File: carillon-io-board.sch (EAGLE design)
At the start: 51 parts, among them J1 22-27-2031-03, J10 22-27-2031-03, J2 22-27-2031-03, J3 22-27-2031-03, J4 22-27-2031-03, J5 22-27-2031-03, J6 22-27-2031-03, J7 22-27-2031-03, J8 22-27-2031-03, J9 22-27-2031-03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

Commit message: fix board
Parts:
- removed R10, R12, R14, R16, R18, R2, R20, R4, R6, R8: (no value), resistor:R-EU_0207/10
- J1, J10, J2, J3, J4, J5, J6, J7, J8, J9: value 22-27-2031-03 -> 22-05-7048-04; device con-molex:22-27-2031-03 -> con-molex:22-05-7048-04
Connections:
- net 12V: now also J1-2.S, J10-2.S, J2-2.S, J3-2.S, J4-2.S, J5-2.S, J6-2.S, J7-2.S, J8-2.S, J9-2.S; no longer J1-1.S, J10-1.S, J2-1.S, J3-1.S, J4-1.S, J5-1.S, J6-1.S, J7-1.S, J8-1.S, J9-1.S
- net GND: now also J1-1.S, J10-1.S, J2-1.S, J3-1.S, J4-1.S, J5-1.S, J6-1.S, J7-1.S, J8-1.S, J9-1.S; no longer R10.2, R12.2, R14.2, R16.2, R18.2, R2.2, R20.2, R4.2, R6.2, R8.2
- net IN1: now also J1-3.S; no longer J1-2.S, R2.1
- net IN10: now also J10-3.S; no longer J10-2.S, R20.1
- net IN2: now also J2-3.S; no longer J2-2.S, R4.1
- net IN3: now also J3-3.S; no longer J3-2.S, R6.1
- net IN4: now also J4-3.S; no longer J4-2.S, R8.1
- net IN5: now also J5-3.S; no longer J5-2.S, R10.1
- net IN6: now also J6-3.S; no longer J6-2.S, R12.1
- net IN7: now also J7-3.S; no longer J7-2.S, R14.1
- net IN8: now also J8-3.S; no longer J8-2.S, R16.1
- net IN9: now also J9-3.S; no longer J9-2.S, R18.1
- net N$1: now also J1-4.S; no longer J1-3.S
- net N$10: now also J10-4.S; no longer J10-3.S
- net N$2: now also J6-4.S; no longer J6-3.S
- net N$3: now also J2-4.S; no longer J2-3.S
- net N$4: now also J3-4.S; no longer J3-3.S
- net N$5: now also J4-4.S; no longer J4-3.S
- net N$6: now also J5-4.S; no longer J5-3.S
- net N$7: now also J7-4.S; no longer J7-3.S
- net N$8: now also J8-4.S; no longer J8-3.S
- net N$9: now also J9-4.S; no longer J9-3.S

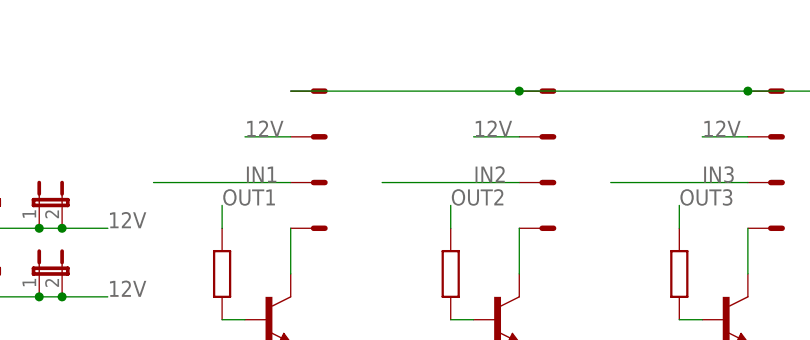
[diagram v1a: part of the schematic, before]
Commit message: io board proved, firmware file added
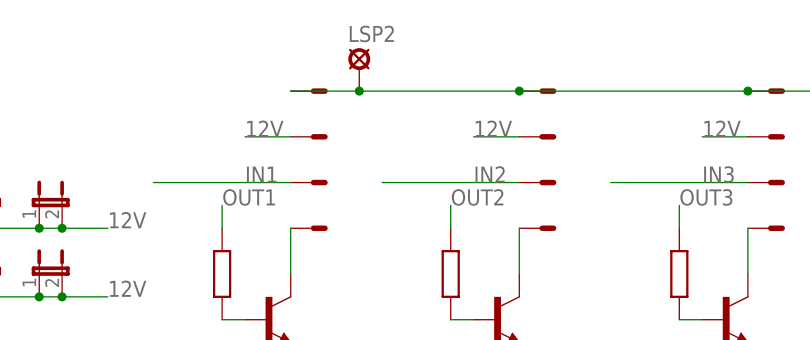
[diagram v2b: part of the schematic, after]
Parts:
- added LSP2: LSP10, solpad:LSP10
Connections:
- net GND: now also LSP2.MP
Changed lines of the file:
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@@
 <part name="J10" library="con-molex" library_urn="urn:adsk.eagle:library:165" deviceset="22-?-04" device="05-7048" package3d_urn="urn:adsk.eagle:package:8078648/1"/>
 <part name="J1" library="con-molex" library_urn="urn:adsk.eagle:library:165" deviceset="22-?-04" device="05-7048" package3d_urn="urn:adsk.eagle:package:8078648/1"/>
+<part name="LSP2" library="solpad" library_urn="urn:adsk.eagle:library:364" deviceset="LSP10" device="" package3d_urn="urn:adsk.eagle:package:26501/1"/>
 </parts>
 <sheets>
@@
 <instance part="J1" gate="-3" x="-114.3" y="78.74" smashed="yes"/>
 <instance part="J1" gate="-4" x="-114.3" y="73.66" smashed="yes"/>
+<instance part="LSP2" gate="1" x="-109.22" y="91.44" smashed="yes">
+<attribute name="NAME" x="-110.49" y="94.361" size="1.778" layer="95"/>
+</instance>
 </instances>
 <busses>
@@
 <pinref part="J2" gate="-1" pin="S"/>
 <wire x1="-2.54" y1="43.18" x2="-2.54" y2="10.16" width="0.1524" layer="91"/>
-<wire x1="-116.84" y1="88.9" x2="-91.44" y2="88.9" width="0.1524" layer="91"/>
+<wire x1="-116.84" y1="88.9" x2="-109.22" y2="88.9" width="0.1524" layer="91"/>
 <pinref part="J3" gate="-1" pin="S"/>
+<wire x1="-109.22" y1="88.9" x2="-91.44" y2="88.9" width="0.1524" layer="91"/>
 <wire x1="-91.44" y1="88.9" x2="-66.04" y2="88.9" width="0.1524" layer="91"/>
 <junction x="-91.44" y="88.9"/>
@@
 <junction x="-2.54" y="43.18"/>
 <pinref part="J1" gate="-1" pin="S"/>
+<pinref part="LSP2" gate="1" pin="MP"/>
+<junction x="-109.22" y="88.9"/>
 </segment>
 </net>
